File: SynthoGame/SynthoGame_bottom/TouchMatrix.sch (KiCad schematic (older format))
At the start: 1 part, among them J9 Touch

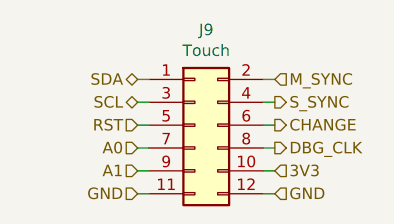
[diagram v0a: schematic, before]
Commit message: Connecting all pins, adding 3D encoder, adding BOM
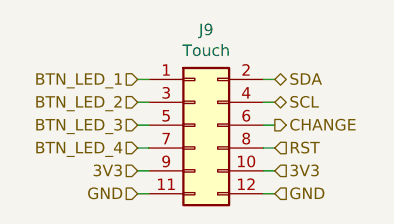
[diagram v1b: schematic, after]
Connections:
- net A1 is gone; now on net 3V3: J9.9 (Pin_9)
- net DBG_CLK is gone; now on net RST: J9.8 (Pin_8)
- net M_SYNC is gone; now on net SDA: J9.2 (Pin_2)
- net S_SYNC is gone; now on net SCL: J9.4 (Pin_4)
- net RST: no longer J9.5 (Pin_5)
- net SCL: no longer J9.3 (Pin_3)
- net SDA: no longer J9.1 (Pin_1)
- net A0 renamed BTN_LED_4
- new net BTN_LED_1: J9.1 (Pin_1)
- new net BTN_LED_2: J9.3 (Pin_3)
- new net BTN_LED_3: J9.5 (Pin_5)
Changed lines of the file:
@@
 	1    0    0    -1
 $EndComp
-Text HLabel 6950 3600 0    50   BiDi ~ 0
+Text HLabel 7550 3600 2    50   BiDi ~ 0
 SDA
-Text HLabel 6950 3700 0    50   BiDi ~ 0
+Text HLabel 7550 3700 2    50   BiDi ~ 0
 SCL
-Text HLabel 6950 3800 0    50   Input ~ 0
+Text HLabel 7550 3900 2    50   Input ~ 0
 RST
-Text HLabel 6950 3900 0    50   Input ~ 0
-A0
-Text HLabel 6950 4000 0    50   Input ~ 0
-A1
-Text HLabel 7550 3600 2    50   Input ~ 0
-M_SYNC
-Text HLabel 7550 3700 2    50   Output ~ 0
-S_SYNC
 Text HLabel 7550 3800 2    50   Output ~ 0
 CHANGE
-Text HLabel 7550 3900 2    50   Output ~ 0
-DBG_CLK
 Text HLabel 7550 4000 2    50   Input ~ 0
 3V3
@@
 Wire Wire Line
 	7500 4100 7550 4100
+Text HLabel 6950 4000 0    50   Input ~ 0
+3V3
+Text HLabel 6950 3600 0    50   Input ~ 0
+BTN_LED_1
+Text HLabel 6950 3700 0    50   Input ~ 0
+BTN_LED_2
+Text HLabel 6950 3800 0    50   Input ~ 0
+BTN_LED_3
+Text HLabel 6950 3900 0    50   Input ~ 0
+BTN_LED_4
 $EndSCHEMATC
